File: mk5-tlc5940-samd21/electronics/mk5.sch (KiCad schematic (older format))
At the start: 54 parts, among them J1 IN/OUT, J10 3, J11 4, J12 5, J13 6, J14 7, J15 8, J16 9, J17 10, J18 11, J19 12, J2 USB, J20 13, J21 14, J22 15, J23 +LED, J24 +LED, J25 +LED, J26 +LED, J27 +LED, J28 Button, J29 GND, J3 15S, J4 GS2, J5 +3V3, J6 +LED, J7 0, J8 1, J9 2, Q1 MOSFET 20V 3A, SW1 BTN, U1 USBLC6-2SC6, U2 MCP1702-3302_SOT23, U3 SAMD11D14A-M, U4 TLC5940PWP

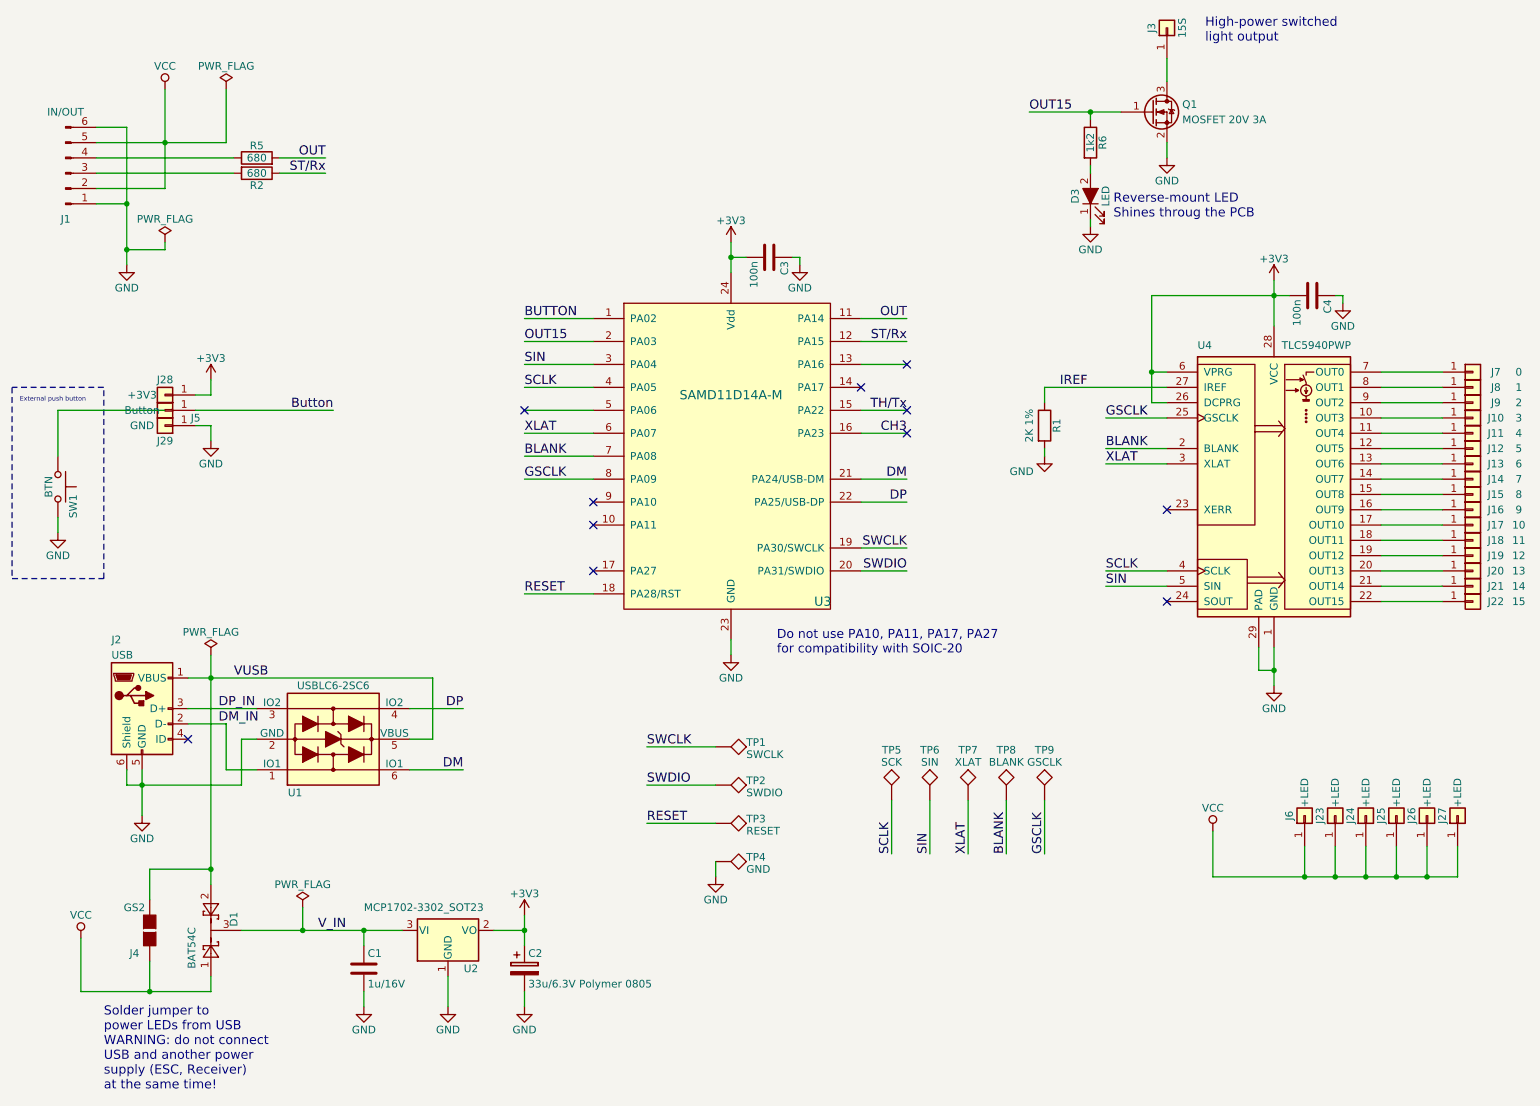
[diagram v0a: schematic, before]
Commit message: New schematics with SAMD21
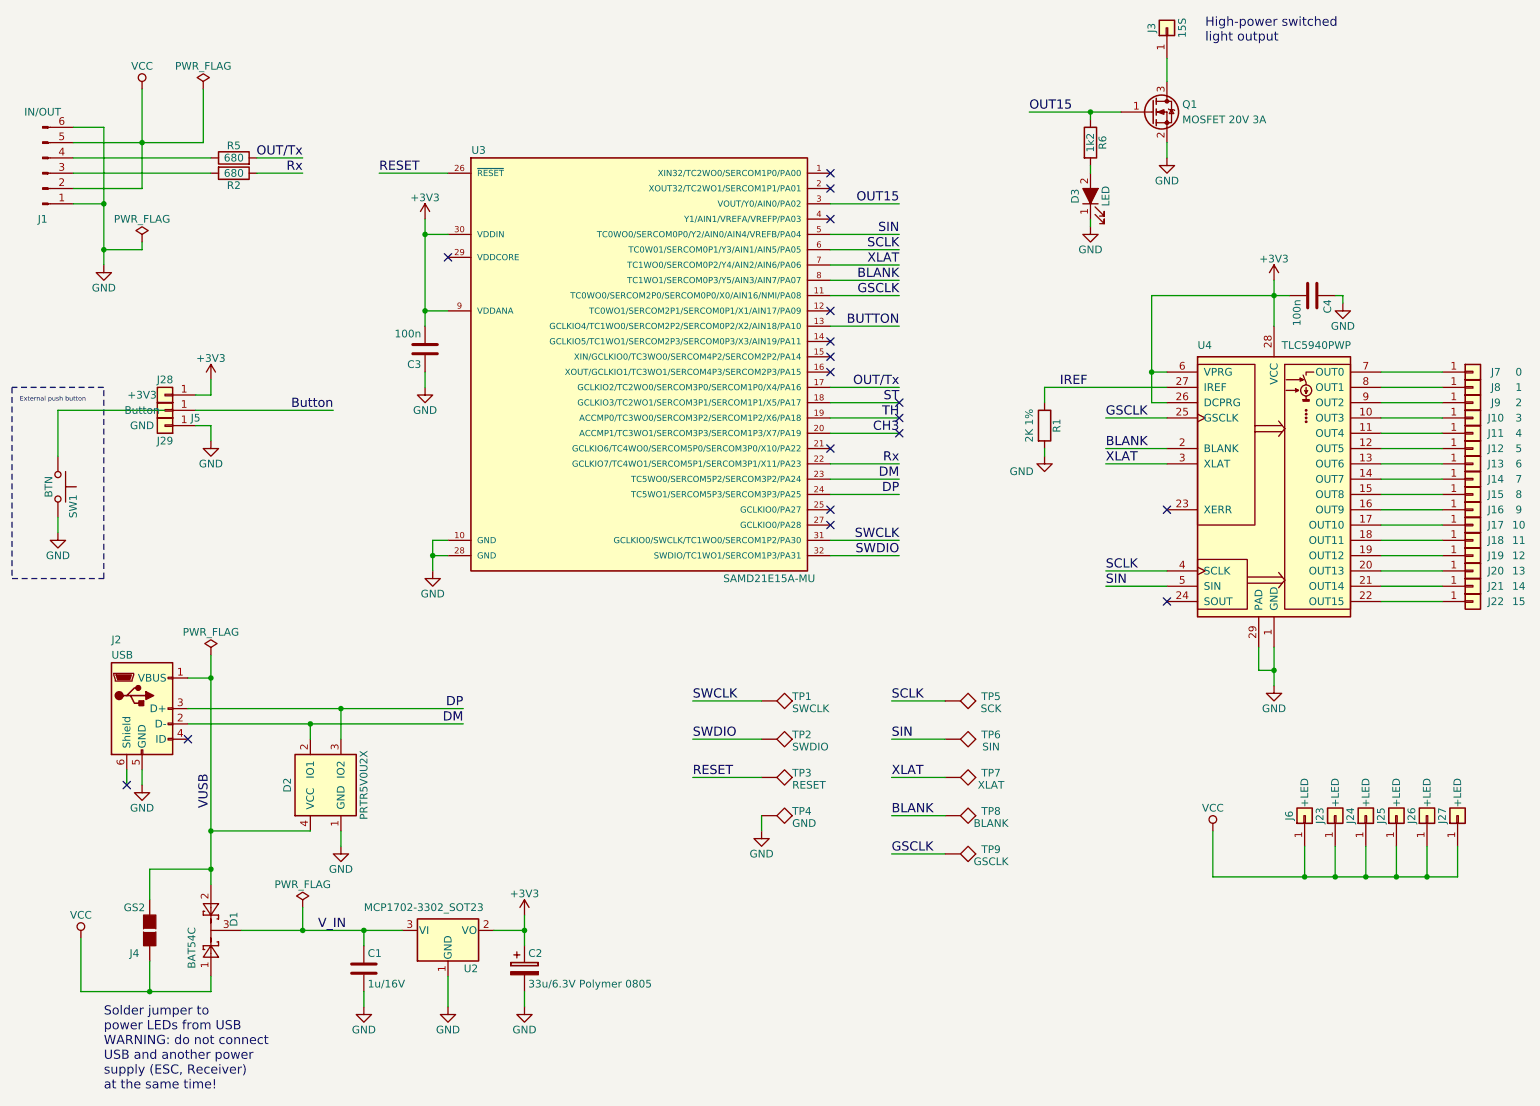
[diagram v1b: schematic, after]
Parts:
- removed U1: USBLC6-2SC6, TO_SOT_Packages_SMD:SOT-23-6, symbol USBLC6-2SC6
- removed U3: SAMD11D14A-M, Housings_DFN_QFN:QFN-24_4x4mm_Pitch0.5mm, symbol SAMD11D14A-M
- added D2: PRTR5V0U2X, symbol PRTR5V0U2X
- added U3: SAMD21E15A-MU, Housings_DFN_QFN:QFN-32-1EP_5x5mm_Pitch0.5mm, symbol SAMD20E15A-MU
- D3: footprint Reverse-LED:REVERSE_MOUNT_ROHM_SLM-81 -> LEDs:LED_0603
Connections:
- net DM_IN is gone; now on net DM: J2.2 (D-)
- net DP_IN is gone; now on net DP: J2.3 (D+)
- net +3V3: now also U3.30 (VDDIN), U3.9 (VDDANA)
- net BLANK: now also U3.8 (TC1WO1/SERCOM0P3/Y5/AIN3/AIN7/PA07)
- net BUTTON: now also U3.13 (GCLKIO4/TC1WO0/SERCOM2P2/SERCOM0P2/X2/AIN18/PA10)
- net CH3: now also U3.20 (ACCMP1/TC3WO1/SERCOM3P3/SERCOM1P3/X7/PA19)
- net DM: now also D2.2 (IO1), U3.23 (TC5WO0/SERCOM5P2/SERCOM3P2/PA24)
- net DP: now also D2.3 (IO2), U3.24 (TC5WO1/SERCOM5P3/SERCOM3P3/PA25)
- net GND: now also D2.1 (GND), U3.10 (GND), U3.28 (GND); no longer J2.6 (Shield)
- net GSCLK: now also U3.11 (TC0WO0/SERCOM2P0/SERCOM0P0/X0/AIN16/NMI/PA08)
- net OUT15: now also U3.3 (VOUT/Y0/AIN0/PA02)
- net RESET: now also U3.26 (~RESET~)
- net SCLK: now also U3.6 (TC0W01/SERCOM0P1/Y3/AIN1/AIN5/PA05)
- net SIN: now also U3.5 (TC0WO0/SERCOM0P0/Y2/AIN0/AIN4/VREFB/PA04)
- net SWCLK: now also U3.31 (GCLKIO0/SWCLK/TC1WO0/SERCOM1P2/PA30)
- net SWDIO: now also U3.32 (SWDIO/TC1WO1/SERCOM1P3/PA31)
- net VUSB: now also D2.4 (VCC)
- net XLAT: now also U3.7 (TC1WO0/SERCOM0P2/Y4/AIN2/AIN6/PA06)
- net OUT renamed OUT/Tx
- net OUT/Tx: now also U3.17 (GCLKIO2/TC2WO0/SERCOM3P0/SERCOM1P0/X4/PA16)
- net ST/Rx renamed Rx
- net Rx: now also U3.22 (GCLKIO7/TC4WO1/SERCOM5P1/SERCOM3P1/X11/PA23)
- new net ST: U3.18 (GCLKIO3/TC2WO1/SERCOM3P1/SERCOM1P1/X5/PA17)
- new net TH: U3.19 (ACCMP0/TC3WO0/SERCOM3P2/SERCOM1P2/X6/PA18)
- no-connect marks 11 -> 18
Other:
- note removed: "Do not use PA10, PA11, PA17, PA27 \nfor compatibility with SOIC-20"
- note removed: "Reverse-mount LED\nShines throug the PCB"
- moved on the sheet: C3, J1, R2, R5, TP1, TP2, TP3, TP4, TP5, TP6, TP7, TP8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

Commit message: Tweak layout
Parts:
- R1: footprint Resistors_SMD:R_0805_HandSoldering -> Resistors_SMD:R_0603
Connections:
- net BUTTON: now also U3.11 (TC0WO0/SERCOM2P0/SERCOM0P0/X0/AIN16/NMI/PA08); no longer U3.13 (GCLKIO4/TC1WO0/SERCOM2P2/SERCOM0P2/X2/AIN18/PA10)
- net GSCLK: now also U3.16 (XOUT/GCLKIO1/TC3WO1/SERCOM4P3/SERCOM2P3/PA15); no longer U3.11 (TC0WO0/SERCOM2P0/SERCOM0P0/X0/AIN16/NMI/PA08)
- net OUT15: now also U3.4 (Y1/AIN1/VREFA/VREFP/PA03); no longer U3.3 (VOUT/Y0/AIN0/PA02)
- net at R2.2: now also J1.4 (Pin_4); no longer J1.3 (Pin_3)
- net at R5.1: now also J1.3 (Pin_3); no longer J1.4 (Pin_4)
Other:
- moved on the sheet: R2, R5
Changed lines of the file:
@@
 F 0 "R1" V 7830 3300 50  0000 C CNN
 F 1 "2K 1%" V 7650 3300 50  0000 C CNN
-F 2 "Resistors_SMD:R_0805_HandSoldering" V 7680 3300 50  0001 C CNN
+F 2 "Resistors_SMD:R_0603" V 7680 3300 50  0001 C CNN
 F 3 "" H 7750 3300 50  0001 C CNN
 	1    7750 3300
@@
 L R R2
 U 1 1 59C50F45
+P 2450 1550
+F 0 "R2" V 2350 1550 50  0000 C CNN
+F 1 "680" V 2450 1550 50  0000 C CNN
+F 2 "Resistors_SMD:R_0603" V 2380 1550 50  0001 C CNN
+F 3 "" H 2450 1550 50  0001 C CNN
+	1    2450 1550
+	0    1    1    0
+$EndComp
+$Comp
+L R R5
+U 1 1 59C512D3
 P 2450 1650
-F 0 "R2" V 2530 1650 50  0000 C CNN
+F 0 "R5" V 2350 1650 50  0000 C CNN
 F 1 "680" V 2450 1650 50  0000 C CNN
 F 2 "Resistors_SMD:R_0603" V 2380 1650 50  0001 C CNN
 F 3 "" H 2450 1650 50  0001 C CNN
 	1    2450 1650
-	0    1    1    0
-$EndComp
-$Comp
-L R R5
-U 1 1 59C512D3
-P 2450 1550
-F 0 "R5" V 2530 1550 50  0000 C CNN
-F 1 "680" V 2450 1550 50  0000 C CNN
-F 2 "Resistors_SMD:R_0603" V 2380 1550 50  0001 C CNN
-F 3 "" H 2450 1550 50  0001 C CNN
-	1    2450 1550
 	0    -1   -1   0
 $EndComp
@@
 Text Label 6800 3050 2    60   ~ 0
 OUT/Tx
+Text Label 2900 1550 2    60   ~ 0
+Rx
 Text Label 2900 1650 2    60   ~ 0
-Rx
-Text Label 2900 1550 2    60   ~ 0
 OUT/Tx
 $Comp
@@
 Text Label 6800 2250 2    60   ~ 0
 XLAT
-Text Label 6800 1850 2    60   ~ 0
+Text Label 6800 1950 2    60   ~ 0
 OUT15
 $Comp
@@
 Text Label 6800 3250 2    60   ~ 0
 TH
-Text Label 6800 2450 2    60   ~ 0
+Text Label 6800 2950 2    60   ~ 0
 GSCLK
 Text Label 6800 4050 2    60   ~ 0
@@
 Text Label 6800 2050 2    60   ~ 0
 SIN
-Text Label 6800 2650 2    60   ~ 0
+Text Label 6800 2450 2    60   ~ 0
 BUTTON
 Text Label 2300 5800 1    60   ~ 0
@@
 	8050 1300 8050 1250
 Connection ~ 8050 1250
-Wire Wire Line
-	6800 2650 6350 2650
 Wire Wire Line
 	1450 7000 2300 7000
@@
 	3700 2950 3700 3050
 Wire Wire Line
-	6350 1850 6800 1850
-Wire Wire Line
 	6350 3050 6800 3050
 Wire Wire Line
@@
 NoConn ~ 6350 2750
 NoConn ~ 6350 2850
-NoConn ~ 6350 2950
 NoConn ~ 6350 3450
 NoConn ~ 6350 3850
@@
 NoConn ~ 6800 3250
 NoConn ~ 6800 3350
-Wire Wire Line
-	6350 2450 6800 2450
-NoConn ~ 6350 1950
 $Comp
 L PRTR5V0U2X D2
@@
 Wire Wire Line
 	3150 5950 3150 6050
+Wire Wire Line
+	6350 1950 6800 1950
+NoConn ~ 6350 1850
+Wire Wire Line
+	6350 2950 6800 2950
+Wire Wire Line
+	6350 2450 6800 2450
+NoConn ~ 6350 2650
 $EndSCHEMATC

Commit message: Add SOT143B, finish layout more or less
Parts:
- D2: footprint (none) -> SOT143B:SOT143B
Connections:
- net DM: now also D2.3 (IO2); no longer D2.2 (IO1)
- net DP: now also D2.2 (IO1); no longer D2.3 (IO2)
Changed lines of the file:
@@
 F 0 "D2" H 3050 5900 50  0000 C CNN
 F 1 "PRTR5V0U2X" H 3050 5400 50  0000 C CNN
-F 2 "" H 3100 5600 50  0001 C CNN
+F 2 "SOT143B:SOT143B" H 3100 5600 50  0001 C CNN
 F 3 "" H 3100 5600 50  0001 C CNN
 	1    3050 5650
 	0    -1   -1   0
 $EndComp
-Wire Wire Line
-	2950 5350 2950 5250
-Connection ~ 2950 5250
-Wire Wire Line
-	3150 5350 3150 5150
-Connection ~ 3150 5150
 Wire Wire Line
 	2300 5950 2950 5950
@@
 	6350 2450 6800 2450
 NoConn ~ 6350 2650
+Wire Wire Line
+	2950 5350 2950 5150
+Connection ~ 2950 5150
+Wire Wire Line
+	3150 5350 3150 5250
+Connection ~ 3150 5250
 $EndSCHEMATC

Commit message: Tweak layout, add C for VCORE
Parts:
- added C5: 1u, Capacitors_SMD:C_0603, symbol C
- C2: value 33u/6.3V Polymer 0805 -> 67u/6.3V Polymer 0805
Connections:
- net GND: now also C5.1
- net VCORE: now reaches U3.29 (VDDCORE)
- net VCORE: now also C5.2
- no-connect marks 18 -> 17
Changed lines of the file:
@@
 P 4350 6850
 F 0 "C2" H 4375 6950 50  0000 L CNN
-F 1 "33u/6.3V Polymer 0805" H 4375 6750 50  0000 L CNN
+F 1 "67u/6.3V Polymer 0805" H 4375 6750 50  0000 L CNN
 F 2 "Capacitors_SMD:C_0805" H 4388 6700 50  0001 C CNN
 F 3 "" H 4350 6850 50  0001 C CNN
@@
 NoConn ~ 6350 3850
 NoConn ~ 6350 3950
-NoConn ~ 3850 2200
 NoConn ~ 6800 3150
 NoConn ~ 6800 3250
@@
 	3150 5350 3150 5250
 Connection ~ 3150 5250
+$Comp
+L C C5
+U 1 1 5A2F6947
+P 3300 2350
+F 0 "C5" H 3325 2450 50  0000 L CNN
+F 1 "1u" H 3325 2250 50  0000 L CNN
+F 2 "Capacitors_SMD:C_0603" H 3338 2200 50  0001 C CNN
+F 3 "" H 3300 2350 50  0001 C CNN
+	1    3300 2350
+	-1   0    0    1
+$EndComp
+$Comp
+L GND #PWR028
+U 1 1 5A2F6A32
+P 3300 2600
+F 0 "#PWR028" H 3300 2350 50  0001 C CNN
+F 1 "GND" H 3300 2450 50  0000 C CNN
+F 2 "" H 3300 2600 50  0001 C CNN
+F 3 "" H 3300 2600 50  0001 C CNN
+	1    3300 2600
+	1    0    0    -1
+$EndComp
+Wire Wire Line
+	3300 2500 3300 2600
+Wire Wire Line
+	3300 2200 3850 2200
+Text Label 3300 2200 0    60   ~ 0
+VCORE
 $EndSCHEMATC

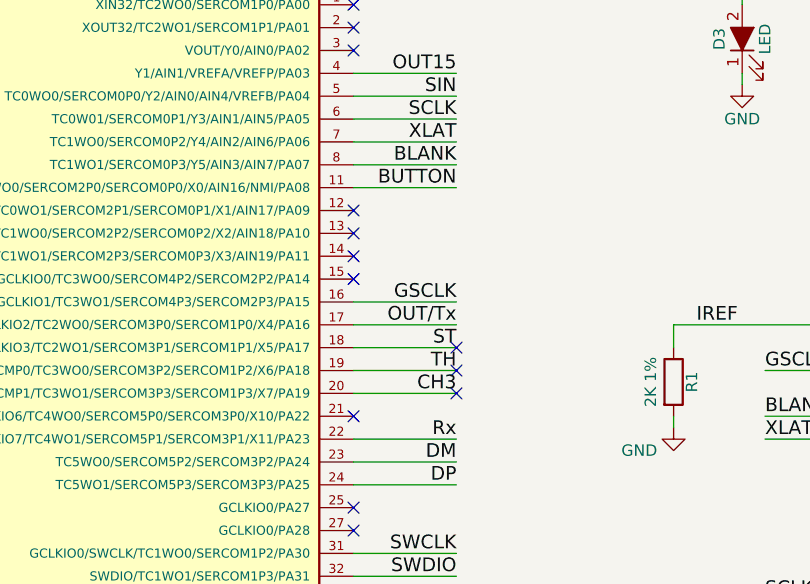
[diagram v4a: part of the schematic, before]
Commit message: Find common pin-out between own hardware and Arduino MKRZero
For the SAM R21 Xplained Pro board we have to use some other
ports and swap the SERCOMs
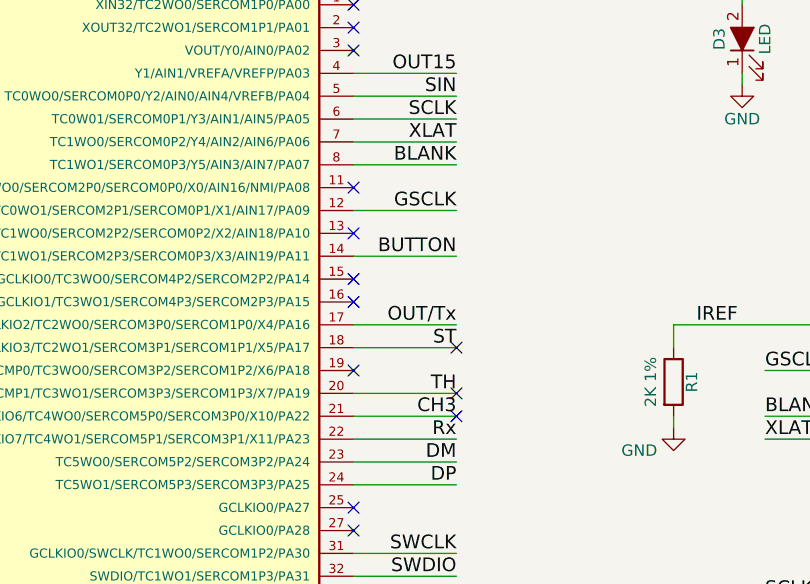
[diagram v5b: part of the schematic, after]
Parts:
- SW1: footprint Buttons_Switches_SMD:SW_SPST_SKQG -> (none)
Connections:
- net BUTTON: now also U3.14 (GCLKIO5/TC1WO1/SERCOM2P3/SERCOM0P3/X3/AIN19/PA11); no longer U3.11 (TC0WO0/SERCOM2P0/SERCOM0P0/X0/AIN16/NMI/PA08)
- net CH3: now also U3.21 (GCLKIO6/TC4WO0/SERCOM5P0/SERCOM3P0/X10/PA22); no longer U3.20 (ACCMP1/TC3WO1/SERCOM3P3/SERCOM1P3/X7/PA19)
- net GSCLK: now also U3.12 (TC0WO1/SERCOM2P1/SERCOM0P1/X1/AIN17/PA09); no longer U3.16 (XOUT/GCLKIO1/TC3WO1/SERCOM4P3/SERCOM2P3/PA15)
- net TH: now also U3.20 (ACCMP1/TC3WO1/SERCOM3P3/SERCOM1P3/X7/PA19); no longer U3.19 (ACCMP0/TC3WO0/SERCOM3P2/SERCOM1P2/X6/PA18)
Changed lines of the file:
@@
 F 0 "SW1" H 1350 3800 50  0000 L CNN
 F 1 "BTN" H 1300 3640 50  0000 C CNN
-F 2 "Buttons_Switches_SMD:SW_SPST_SKQG" H 1300 3900 50  0001 C CNN
+F 2 "" H 1300 3900 50  0001 C CNN
 F 3 "" H 1300 3900 50  0001 C CNN
 	1    1300 3700
@@
 Text Label 6800 2350 2    60   ~ 0
 BLANK
-Text Label 6800 3250 2    60   ~ 0
+Text Label 6800 3350 2    60   ~ 0
 TH
-Text Label 6800 2950 2    60   ~ 0
+Text Label 6800 2550 2    60   ~ 0
 GSCLK
 Text Label 6800 4050 2    60   ~ 0
@@
 Text Label 3400 1650 0    60   ~ 0
 RESET
-Text Label 6800 3350 2    60   ~ 0
+Text Label 6800 3450 2    60   ~ 0
 CH3
 $Comp
@@
 Text Label 6800 2050 2    60   ~ 0
 SIN
-Text Label 6800 2450 2    60   ~ 0
+Text Label 6800 2750 2    60   ~ 0
 BUTTON
 Text Label 2300 5800 1    60   ~ 0
@@
 	6350 3150 6800 3150
 Wire Wire Line
-	6350 3250 6800 3250
-Wire Wire Line
 	6350 3350 6800 3350
 NoConn ~ 6350 1650
 NoConn ~ 6350 1750
-NoConn ~ 6350 2550
-NoConn ~ 6350 2750
 NoConn ~ 6350 2850
-NoConn ~ 6350 3450
 NoConn ~ 6350 3850
 NoConn ~ 6350 3950
 NoConn ~ 6800 3150
-NoConn ~ 6800 3250
+NoConn ~ 6350 3250
 NoConn ~ 6800 3350
 $Comp
@@
 NoConn ~ 6350 1850
 Wire Wire Line
-	6350 2950 6800 2950
-Wire Wire Line
-	6350 2450 6800 2450
-NoConn ~ 6350 2650
-Wire Wire Line
 	2950 5350 2950 5150
 Connection ~ 2950 5150
@@
 Text Label 3300 2200 0    60   ~ 0
 VCORE
+Wire Wire Line
+	6350 3450 6800 3450
+NoConn ~ 6800 3450
+Wire Wire Line
+	6350 2750 6800 2750
+NoConn ~ 6350 2450
+NoConn ~ 6350 2950
+NoConn ~ 6350 2650
+Wire Wire Line
+	6350 2550 6800 2550
 $EndSCHEMATC

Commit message: Optimize pins we we don't need TCC0/W pins for input capture
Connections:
- net CH3: now also U3.18 (GCLKIO3/TC2WO1/SERCOM3P1/SERCOM1P1/X5/PA17); no longer U3.21 (GCLKIO6/TC4WO0/SERCOM5P0/SERCOM3P0/X10/PA22)
- net OUT/Tx: now also U3.21 (GCLKIO6/TC4WO0/SERCOM5P0/SERCOM3P0/X10/PA22); no longer U3.17 (GCLKIO2/TC2WO0/SERCOM3P0/SERCOM1P0/X4/PA16)
- net ST: now also U3.17 (GCLKIO2/TC2WO0/SERCOM3P0/SERCOM1P0/X4/PA16); no longer U3.18 (GCLKIO3/TC2WO1/SERCOM3P1/SERCOM1P1/X5/PA17)
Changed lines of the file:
@@
 	0    -1   -1   0
 $EndComp
-Text Label 6800 3150 2    60   ~ 0
+Text Label 6800 3050 2    60   ~ 0
 ST
-Text Label 6800 3050 2    60   ~ 0
+Text Label 6800 3450 2    60   ~ 0
 OUT/Tx
 Text Label 2900 1550 2    60   ~ 0
@@
 Text Label 3400 1650 0    60   ~ 0
 RESET
-Text Label 6800 3450 2    60   ~ 0
+Text Label 6800 3150 2    60   ~ 0
 CH3
 $Comp
@@
 VCORE
 Wire Wire Line
-	6350 3450 6800 3450
-NoConn ~ 6800 3450
-Wire Wire Line
 	6350 2750 6800 2750
 NoConn ~ 6350 2450
@@
 Wire Wire Line
 	6350 2550 6800 2550
+Wire Wire Line
+	6350 3450 6800 3450
+NoConn ~ 6800 3050
 $EndSCHEMATC

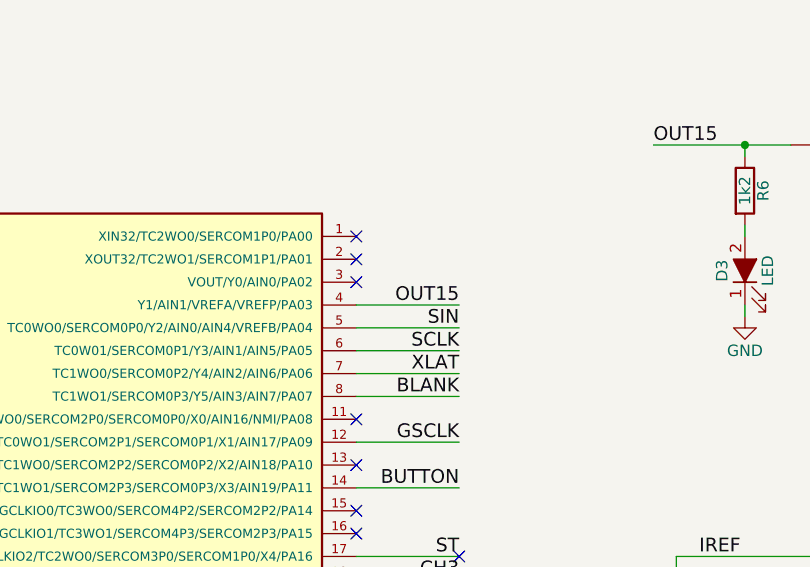
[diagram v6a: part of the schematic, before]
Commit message: OUT15S moved from PA03 to PA02, as PA03 has large cap on Arduino (AREF)
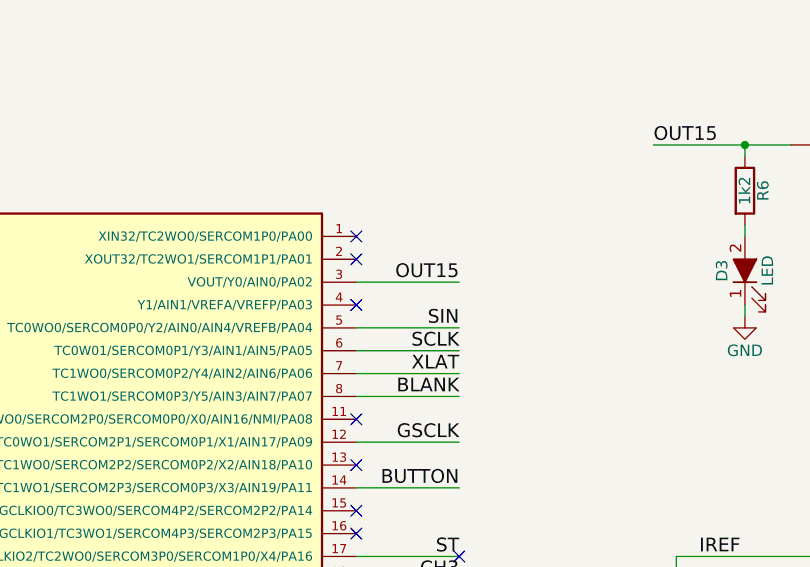
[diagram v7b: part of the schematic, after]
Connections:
- net OUT15: now also U3.3 (VOUT/Y0/AIN0/PA02); no longer U3.4 (Y1/AIN1/VREFA/VREFP/PA03)
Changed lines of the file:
@@
 Text Label 6800 2250 2    60   ~ 0
 XLAT
-Text Label 6800 1950 2    60   ~ 0
+Text Label 6800 1850 2    60   ~ 0
 OUT15
 $Comp
@@
 	3150 5950 3150 6050
 Wire Wire Line
-	6350 1950 6800 1950
-NoConn ~ 6350 1850
-Wire Wire Line
 	2950 5350 2950 5150
 Connection ~ 2950 5150
@@
 	6350 3450 6800 3450
 NoConn ~ 6800 3050
+Wire Wire Line
+	6350 1850 6800 1850
+NoConn ~ 6350 1950
 $EndSCHEMATC
